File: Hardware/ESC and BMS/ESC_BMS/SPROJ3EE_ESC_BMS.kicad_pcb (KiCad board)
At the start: 2 copper layers, 100 x 40 mm, 0 parts

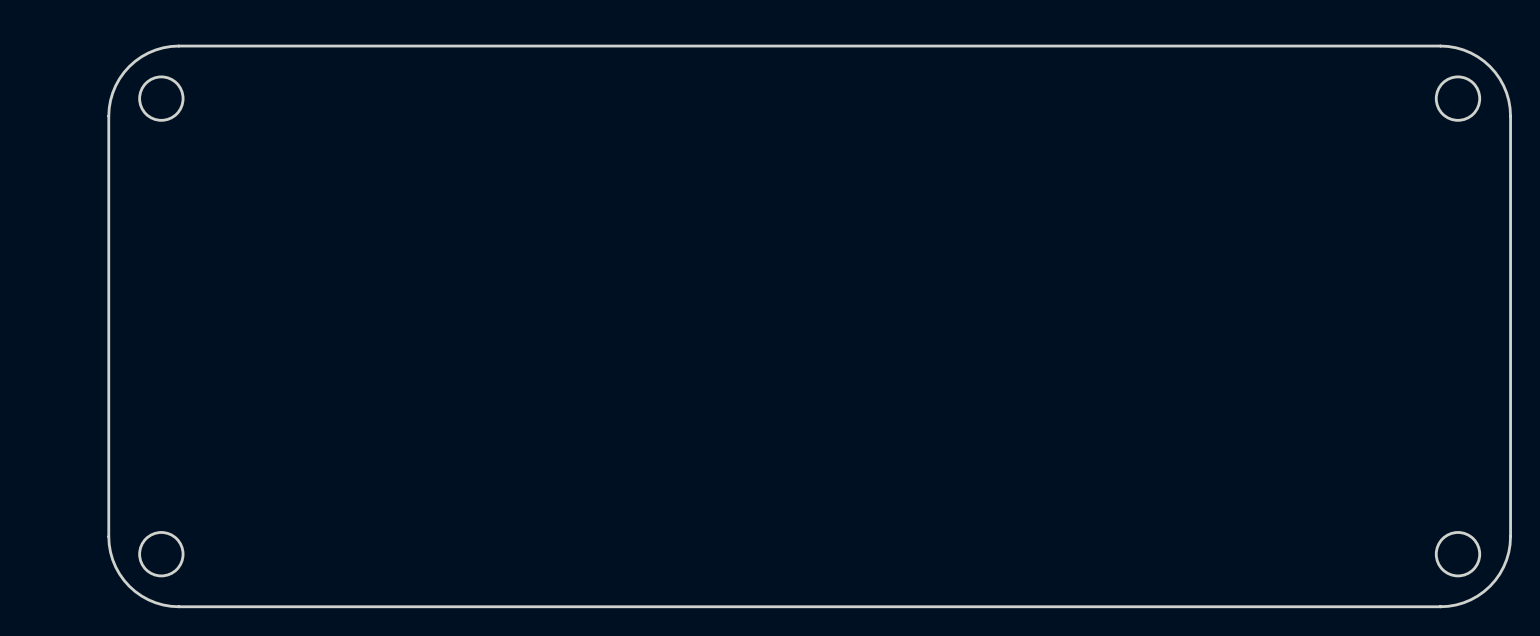
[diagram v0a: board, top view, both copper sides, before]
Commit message: ESC/BMS PCB started
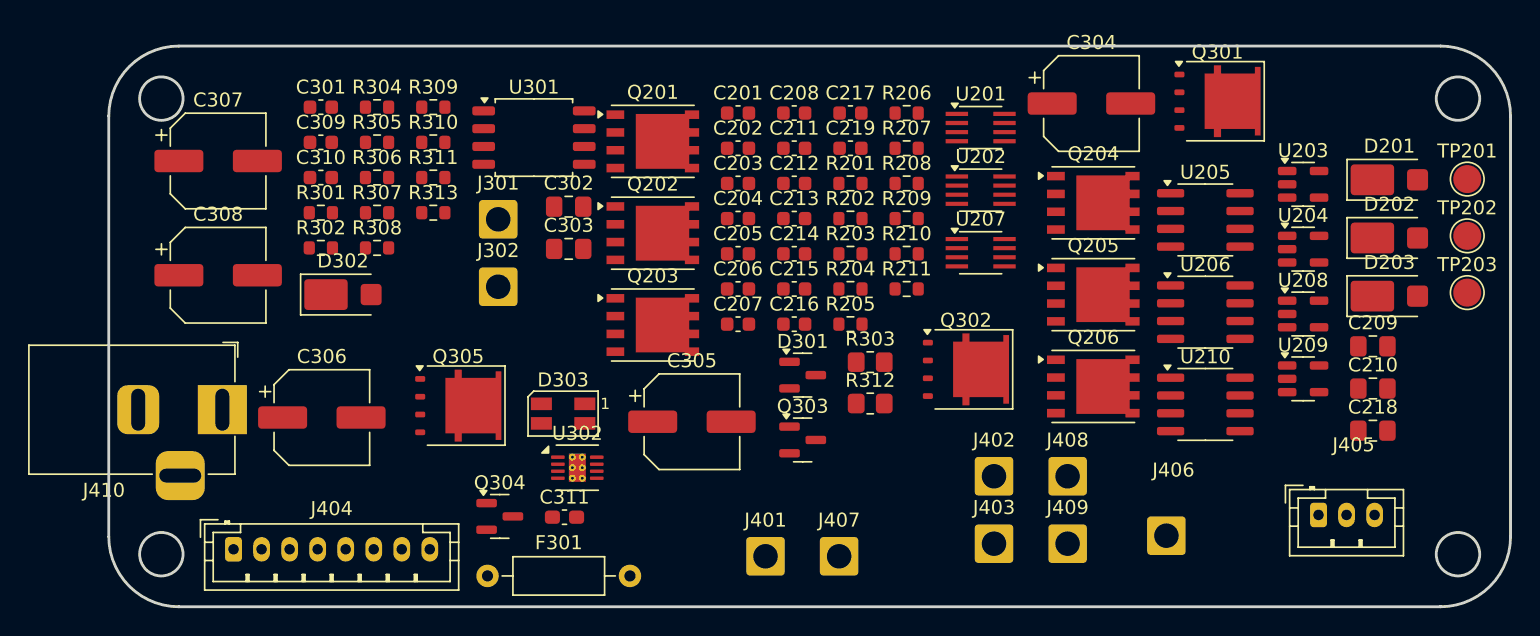
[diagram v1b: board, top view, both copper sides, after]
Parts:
- added C201: 100n, Capacitor_SMD:C_0603_1608Metric, F.Cu at (139.9, 75.1)
- added C202: 100n, Capacitor_SMD:C_0603_1608Metric, F.Cu at (139.9, 77.6)
- added C203: 100n, Capacitor_SMD:C_0603_1608Metric, F.Cu at (139.9, 80.1)
- added C204: 100n, Capacitor_SMD:C_0603_1608Metric, F.Cu at (139.9, 82.6)
- added C205: 100n, Capacitor_SMD:C_0603_1608Metric, F.Cu at (139.9, 85.1)
- added C206: 100n, Capacitor_SMD:C_0603_1608Metric, F.Cu at (139.9, 87.6)
- added C207: 1u, Capacitor_SMD:C_0603_1608Metric, F.Cu at (139.9, 90.1)
- added C208: 1u, Capacitor_SMD:C_0603_1608Metric, F.Cu at (143.9, 75.1)
- added C209: 22u, Capacitor_SMD:C_0805_2012Metric_Pad1.18x1.45mm_HandSolder, F.Cu at (185.2, 91.7)
- added C210: 22u, Capacitor_SMD:C_0805_2012Metric_Pad1.18x1.45mm_HandSolder, F.Cu at (185.2, 94.7)
- added C211: 1u, Capacitor_SMD:C_0603_1608Metric, F.Cu at (143.9, 77.6)
- added C212: 1u, Capacitor_SMD:C_0603_1608Metric, F.Cu at (143.9, 80.1)
- added C213: 100n, Capacitor_SMD:C_0603_1608Metric, F.Cu at (143.9, 82.6)
- added C214: 100n, Capacitor_SMD:C_0603_1608Metric, F.Cu at (143.9, 85.1)
- added C215: 100n, Capacitor_SMD:C_0603_1608Metric, F.Cu at (143.9, 87.6)
- added C216: 100n, Capacitor_SMD:C_0603_1608Metric, F.Cu at (143.9, 90.1)
- added C217: 1u, Capacitor_SMD:C_0603_1608Metric, F.Cu at (147.9, 75.1)
- added C218: 22u, Capacitor_SMD:C_0805_2012Metric_Pad1.18x1.45mm_HandSolder, F.Cu at (185.2, 97.7)
- added C219: 1u, Capacitor_SMD:C_0603_1608Metric, F.Cu at (147.9, 77.6)
- added C301: 100n, Capacitor_SMD:C_0603_1608Metric, F.Cu at (110.1, 74.7)
- added C302: 100n, Capacitor_SMD:C_0805_2012Metric_Pad1.18x1.45mm_HandSolder, F.Cu at (127.8, 81.8)
- added C303: 100n, Capacitor_SMD:C_0805_2012Metric_Pad1.18x1.45mm_HandSolder, F.Cu at (127.8, 84.8)
- added C304: 220µ, Capacitor_SMD:CP_Elec_6.3x5.9, F.Cu at (165.1, 74.4)
- added C305: 220µ, Capacitor_SMD:CP_Elec_6.3x5.9, F.Cu at (136.6, 97.1)
- added C306: 220µ, Capacitor_SMD:CP_Elec_6.3x5.9, F.Cu at (110.2, 96.8)
- added C307: 220µ, Capacitor_SMD:CP_Elec_6.3x5.9, F.Cu at (102.8, 78.5)
- added C308: 220µ, Capacitor_SMD:CP_Elec_6.3x5.9, F.Cu at (102.8, 86.7)
- added C309: 100n, Capacitor_SMD:C_0603_1608Metric, F.Cu at (110.1, 77.2)
- added C310: 100n, Capacitor_SMD:C_0603_1608Metric, F.Cu at (110.1, 79.7)
- added C311: 470nF, Capacitor_SMD:C_0603_1608Metric_Pad1.08x0.95mm_HandSolder, F.Cu at (127.5, 103.9)
- added D201: MSS1P3L-M3/89A, Diode_SMD:Vishay_SMPA, F.Cu at (186.4, 79.8)
- added D202: MSS1P3L-M3/89A, Diode_SMD:Vishay_SMPA, F.Cu at (186.4, 84.0)
- added D203: MSS1P3L-M3/89A, Diode_SMD:Vishay_SMPA, F.Cu at (186.4, 88.1)
- added D301: BZX84B, Package_TO_SOT_SMD:SOT-23, F.Cu at (144.5, 93.8)
- added D302: MSS1P3L-M3/89A, Diode_SMD:Vishay_SMPA, F.Cu at (111.7, 88.0)
- added D303: 150141RV73100, LED_SMD:LED_RGB_Wuerth-PLCC4_3.2x2.8mm_150141M173100, F.Cu at (127.4, 96.5)
- added F301: RUEF Polyfuse, Resistor_THT:R_Axial_DIN0207_L6.3mm_D2.5mm_P10.16mm_Horizontal, F.Cu at (122.0, 108.1)
- added J301: SW IN, Connector_Wire:SolderWire-1sqmm_1x01_D1.4mm_OD2.7mm, F.Cu at (122.8, 82.7)
- added J302: SW OUT, Connector_Wire:SolderWire-1sqmm_1x01_D1.4mm_OD2.7mm, F.Cu at (122.8, 87.5)
- added J401: 1mm2_connector, Connector_Wire:SolderWire-1sqmm_1x01_D1.4mm_OD2.7mm, F.Cu at (141.8, 106.7)
- added J402: 1mm2_connector, Connector_Wire:SolderWire-1sqmm_1x01_D1.4mm_OD2.7mm, F.Cu at (158.2, 101.0)
- added J403: 1mm2_connector, Connector_Wire:SolderWire-1sqmm_1x01_D1.4mm_OD2.7mm, F.Cu at (158.2, 105.8)
- added J404: JST_8PH_2mm, Connector_JST:JST_PH_B8B-PH-K_1x08_P2.00mm_Vertical, F.Cu at (103.9, 106.2)
- added J405: JST_3PH_2mm, Connector_JST:JST_PH_B3B-PH-K_1x03_P2.00mm_Vertical, F.Cu at (181.3, 103.8)
- added J406: 1mm2_connector, Connector_Wire:SolderWire-1sqmm_1x01_D1.4mm_OD2.7mm, F.Cu at (170.4, 105.2)
- added J407: 1mm2_connector, Connector_Wire:SolderWire-1sqmm_1x01_D1.4mm_OD2.7mm, F.Cu at (147.1, 106.7)
- added J408: 1mm2_connector, Connector_Wire:SolderWire-1sqmm_1x01_D1.4mm_OD2.7mm, F.Cu at (163.4, 101.0)
- added J409: 1mm2_connector, Connector_Wire:SolderWire-1sqmm_1x01_D1.4mm_OD2.7mm, F.Cu at (163.4, 105.8)
- added J410: Jack-DC, Connector_BarrelJack:BarrelJack_Horizontal, F.Cu at (103.1, 96.2)
- added Q201: SiR696DP, Package_SO:PowerPAK_SO-8_Single, F.Cu at (133.8, 77.1)
- added Q202: SiR696DP, Package_SO:PowerPAK_SO-8_Single, F.Cu at (133.8, 83.7)
- added Q203: SiR696DP, Package_SO:PowerPAK_SO-8_Single, F.Cu at (133.8, 90.2)
- added Q204: SiR696DP, Package_SO:PowerPAK_SO-8_Single, F.Cu at (165.2, 81.5)
- added Q205: SiR696DP, Package_SO:PowerPAK_SO-8_Single, F.Cu at (165.2, 88.0)
- added Q206: SiR696DP, Package_SO:PowerPAK_SO-8_Single, F.Cu at (165.2, 94.6)
- added Q301: SQJ141ELP, Package_SO:PowerPAK_SO-8L_Single, F.Cu at (174.1, 74.2)
- added Q302: SQJ141ELP, Package_SO:PowerPAK_SO-8L_Single, F.Cu at (156.1, 93.4)
- added Q303: FDV304P, Package_TO_SOT_SMD:SOT-23, F.Cu at (144.5, 98.4)
- added Q304: PMV20XNEA, Package_TO_SOT_SMD:SOT-23, F.Cu at (122.9, 103.9)
- added Q305: SQJ141ELP, Package_SO:PowerPAK_SO-8L_Single, F.Cu at (119.9, 96.0)
- added R201: 47R, Resistor_SMD:R_0603_1608Metric, F.Cu at (147.9, 80.1)
- added R202: 47R, Resistor_SMD:R_0603_1608Metric, F.Cu at (147.9, 82.6)
- added R203: 47R, Resistor_SMD:R_0603_1608Metric, F.Cu at (147.9, 85.1)
- added R204: 47R, Resistor_SMD:R_0603_1608Metric, F.Cu at (147.9, 87.6)
- added R205: 47k, Resistor_SMD:R_0603_1608Metric, F.Cu at (147.9, 90.1)
- added R206: 47k, Resistor_SMD:R_0603_1608Metric, F.Cu at (151.9, 75.1)
- added R207: 47k, Resistor_SMD:R_0603_1608Metric, F.Cu at (151.9, 77.6)
- added R208: 47k, Resistor_SMD:R_0603_1608Metric, F.Cu at (151.9, 80.1)
- added R209: 1k, Resistor_SMD:R_0603_1608Metric, F.Cu at (151.9, 82.6)
- added R210: 47R, Resistor_SMD:R_0603_1608Metric, F.Cu at (151.9, 85.1)
- added R211: 47R, Resistor_SMD:R_0603_1608Metric, F.Cu at (151.9, 87.6)
- added R301: 27k, Resistor_SMD:R_0603_1608Metric, F.Cu at (110.1, 82.2)
- added R302: 10k, Resistor_SMD:R_0603_1608Metric, F.Cu at (110.1, 84.7)
- added R303: 120m, Resistor_SMD:R_0805_2012Metric_Pad1.20x1.40mm_HandSolder, F.Cu at (149.3, 92.8)
- added R304: 10k, Resistor_SMD:R_0603_1608Metric, F.Cu at (114.1, 74.7)
- added R305: 1k, Resistor_SMD:R_0603_1608Metric, F.Cu at (114.1, 77.2)
- added R306: 1k, Resistor_SMD:R_0603_1608Metric, F.Cu at (114.1, 79.7)
- added R307: 1k, Resistor_SMD:R_0603_1608Metric, F.Cu at (114.1, 82.2)
- added R308: 1k, Resistor_SMD:R_0603_1608Metric, F.Cu at (114.1, 84.7)
- added R309: 1k, Resistor_SMD:R_0603_1608Metric, F.Cu at (118.2, 74.7)
- added R310: 1k, Resistor_SMD:R_0603_1608Metric, F.Cu at (118.2, 77.2)
- added R311: 100, Resistor_SMD:R_0603_1608Metric, F.Cu at (118.2, 79.7)
- added R312: 1M, Resistor_SMD:R_0805_2012Metric_Pad1.20x1.40mm_HandSolder, F.Cu at (149.3, 95.8)
- added R313: 10k, Resistor_SMD:R_0603_1608Metric, F.Cu at (118.2, 82.2)
- added TP201: TestPoint, TestPoint:TestPoint_Pad_D2.0mm, F.Cu at (191.9, 79.8)
- added TP202: TestPoint, TestPoint:TestPoint_Pad_D2.0mm, F.Cu at (191.9, 83.8)
- added TP203: TestPoint, TestPoint:TestPoint_Pad_D2.0mm, F.Cu at (191.9, 87.9)
- added U201: 74AUC2G08, Package_SO:SSOP-8_2.95x2.8mm_P0.65mm, F.Cu at (157.2, 76.1)
- added U202: 74AUC2G08, Package_SO:SSOP-8_2.95x2.8mm_P0.65mm, F.Cu at (157.2, 80.6)
- added U203: SN74LVC1G00DBV, Package_TO_SOT_SMD:SOT-23-5, F.Cu at (180.2, 80.2)
- added U204: SN74LVC1G00DBV, Package_TO_SOT_SMD:SOT-23-5, F.Cu at (180.2, 84.8)
- added U205: IR2301, Package_SO:SOIC-8_3.9x4.9mm_P1.27mm, F.Cu at (173.2, 82.7)
- added U206: IR2301, Package_SO:SOIC-8_3.9x4.9mm_P1.27mm, F.Cu at (173.2, 89.3)
- added U207: 74AUC2G08, Package_SO:SSOP-8_2.95x2.8mm_P0.65mm, F.Cu at (157.2, 85.0)
- added U208: SN74LVC1G00DBV, Package_TO_SOT_SMD:SOT-23-5, F.Cu at (180.2, 89.4)
- added U209: TL331, Package_TO_SOT_SMD:SOT-23-5, F.Cu at (180.2, 94.0)
- added U210: IR2301, Package_SO:SOIC-8_3.9x4.9mm_P1.27mm, F.Cu at (173.2, 95.9)
- added U301: BQ2057W, Package_SO:SOIC-8_5.3x5.3mm_P1.27mm, F.Cu at (125.3, 76.8)
- added U302: BQ2969, Package_SON:WSON-8-1EP_3x3mm_P0.5mm_EP1.2x2mm_ThermalVias, F.Cu at (128.4, 100.4)

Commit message: PCB component placement init
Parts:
- moved R303 118.2 mm to (57.0, 166.8), turned to 90 degrees
- moved R305 113.2 mm to (58.5, 175.7), turned to 90 degrees
- moved Q302 112.8 mm to (61.0, 154.1)
- moved R304 111.2 mm to (63.6, 173.8), turned to 180 degrees
- moved C303 110.4 mm to (60.9, 172.6), turned to 90 degrees
- moved U301 110.1 mm to (63.0, 167.5)
- moved R306 104.8 mm to (66.3, 172.9), turned to 90 degrees
- moved D302 100.8 mm to (62.9, 176.2), turned to 180 degrees
- moved R310 99.5 mm to (74.7, 166.7), turned to 90 degrees
- moved R302 99.0 mm to (63.7, 172.1)
- moved C307 98.5 mm to (149.2, 165.4), turned to -90 degrees
- moved J404 98.3 mm to (186.4, 52.7), turned to 180 degrees
- moved R307 97.7 mm to (68.7, 168.6), turned to -90 degrees
- moved C301 92.1 mm to (154.9, 155.2), turned to 180 degrees
- moved C304 91.3 mm to (157.1, 165.3), turned to -90 degrees
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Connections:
- C303 pad 1: GND -> VCC
- D302 pad 2: /2. BMS/DC -> VCC
- R305 pad 1: /2. BMS/DC -> VCC
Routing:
- net Net-(Q303-D): track 0.00 -> 26.7 mm, vias 0 -> 2
- net Net-(Q305-D): track 0.00 -> 20.7 mm, vias 0 -> 2
- net Net-(Q303-G): track 0.00 -> 11.9 mm
- net +VPROT: track 0.00 -> 11.2 mm
- net Net-(U302-V1): track 0.00 -> 10.5 mm, vias 0 -> 2
- net Net-(Q304-G): track 0.00 -> 6.56 mm
- net Net-(Q303-S): track 0.00 -> 4.14 mm
- net Net-(U302-V2): track 0.00 -> 3.08 mm
- net VDD: track 0.00 -> 3.03 mm
- net Net-(U302-CTL): track 0.00 -> 3.02 mm
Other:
- copper layers 2 -> 4

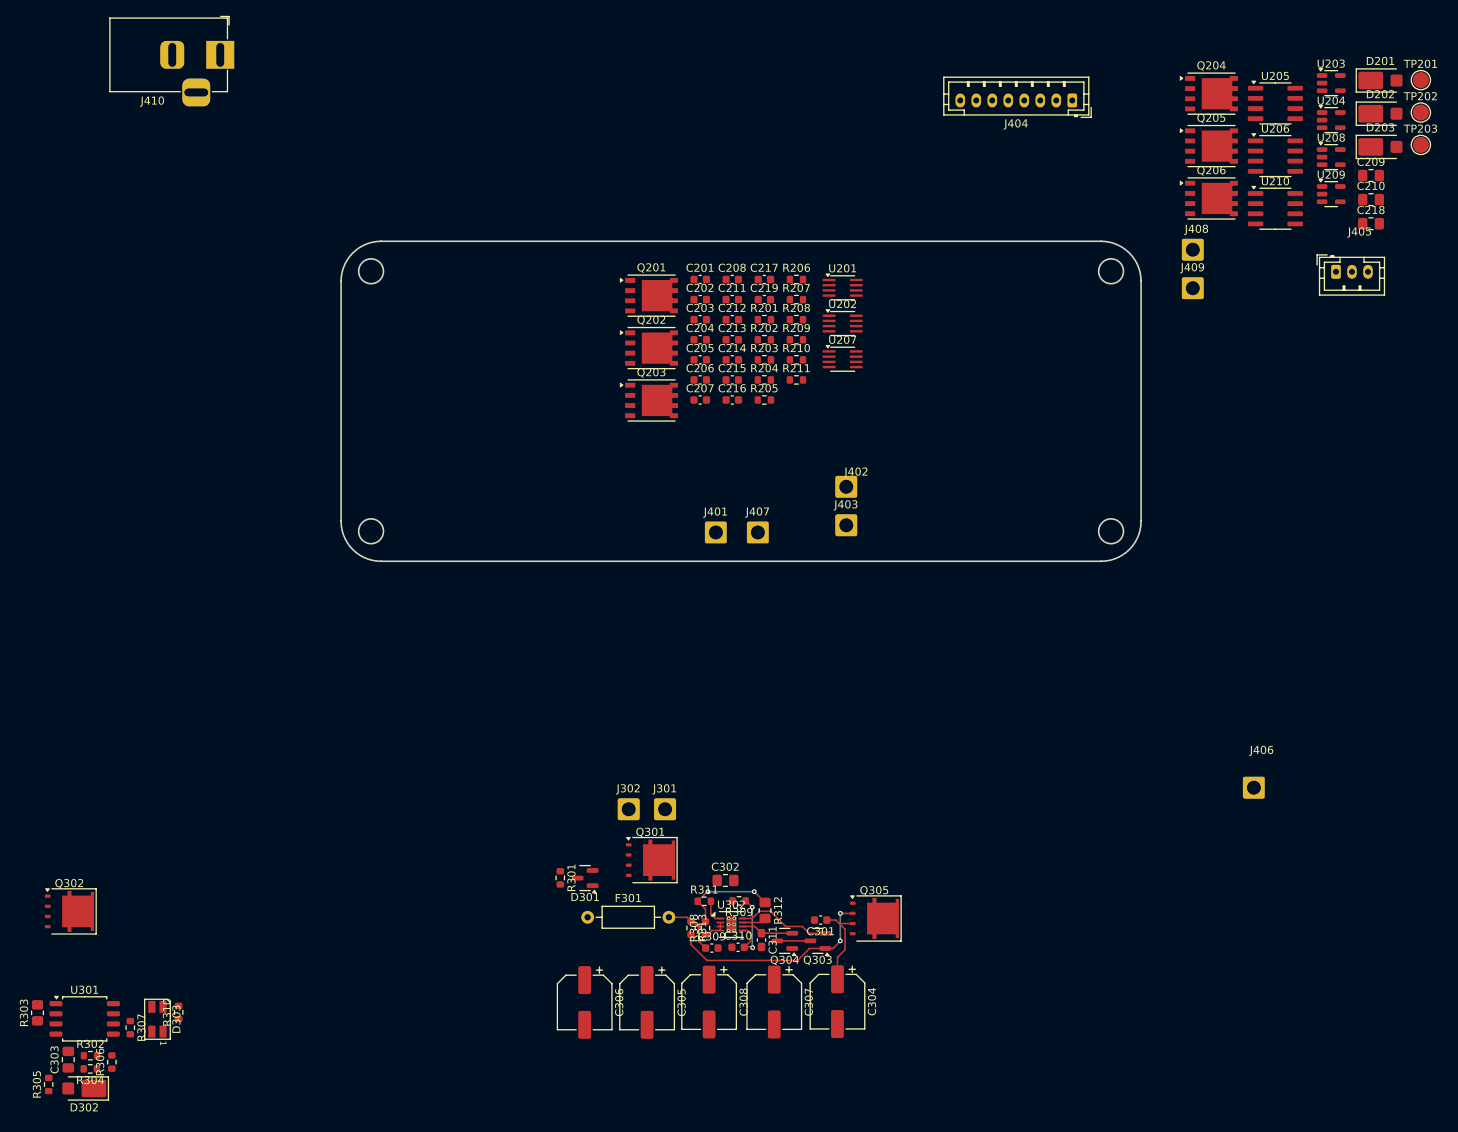
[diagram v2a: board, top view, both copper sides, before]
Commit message: ESC BMS component placement close to done
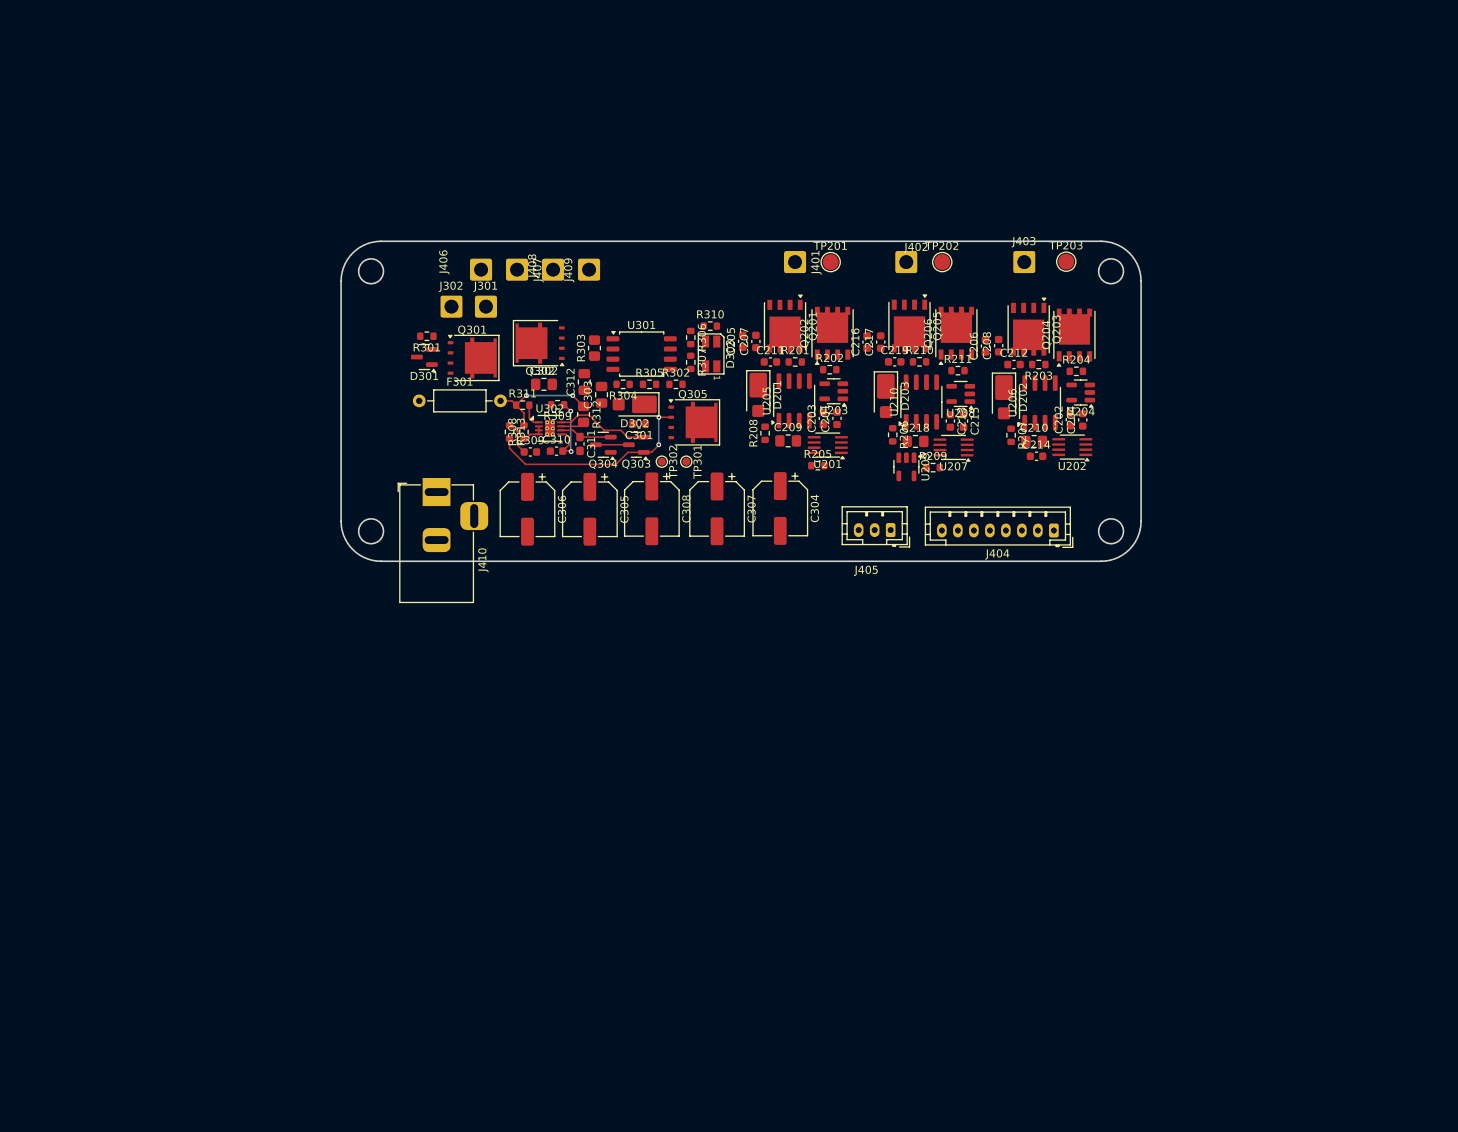
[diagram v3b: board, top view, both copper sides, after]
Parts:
- added C312: 100n, Capacitor_SMD:C_0805_2012Metric_Pad1.18x1.45mm_HandSolder, F.Cu at (125.4, 87.9)
- added TP301: TestPoint, TestPoint:TestPoint_Pad_D1.0mm, F.Cu at (138.2, 97.8)
- added TP302: TestPoint, TestPoint:TestPoint_Pad_D1.0mm, F.Cu at (135.1, 97.8)
- J410: value Jack-DC -> Barrel_Jack_Switch
- moved J406 116.3 mm to (112.5, 73.8), turned to 90 degrees
- moved R306 115.9 mm to (138.7, 82.3), turned to -90 degrees
- moved R305 115.3 mm to (133.6, 88.2), turned to 0 degrees
- moved R302 111.3 mm to (136.9, 88.2)
- moved D302 109.8 mm to (131.7, 90.7)
- moved R307 108.7 mm to (138.7, 85.4)
- moved R310 108.5 mm to (141.2, 80.9), turned to 0 degrees
- moved R304 108.4 mm to (130.3, 88.2)
- moved R303 108.4 mm to (126.7, 83.7)
- moved U301 108.4 mm to (132.6, 84.4)
- moved D303 108.2 mm to (141.3, 84.4)
- moved C303 106.5 mm to (127.6, 89.5)
- moved Q302 92.2 mm to (119.9, 83.0), turned to 180 degrees
- moved D201 87.1 mm to (147.2, 89.5), turned to -90 degrees
- moved C209 80.1 mm to (150.9, 95.2)
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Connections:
- D302 pad 2: VCC -> +VCHARGE
- J410 pad 1: /3. Connectors/DC -> +VCHARGE
- J410 pad 3: (no net) -> GND
- R305 pad 1: VCC -> +VCHARGE
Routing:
- net +VPROT: track 11.2 -> 0.00 mm
- net Net-(Q305-D): track 20.7 -> 19.9 mm
- added copper zone on In2.Cu, net +VPROT
- added copper zone on In1.Cu, net GND
